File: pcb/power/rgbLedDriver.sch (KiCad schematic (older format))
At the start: 39 parts, among them Q1 MMBT3904, Q2 MMBT3904, Q3 MMBT3904, Q4 MMBT3904, Q5 MMBT3904, Q6 MMBT3904, Q7 DMG2305UX, Q8 DMG2305UX, Q9 DMG2305UX

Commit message: Did a lot of stuff. Currently working on the exact 3D models for the headers.
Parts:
- R21, R22, R23, R24, R25, R26, R30, R31, R32: footprint Resistors_SMD:R_0603_HandSoldering -> Additional:R_0603_HandSoldering_Same_As_C
- R27, R28, R29: footprint Capacitors_SMD:C_0603_HandSoldering -> Additional:R_0603_HandSoldering_Same_As_C
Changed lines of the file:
@@
 F 0 "R24" V 2680 1350 50  0000 C CNN
 F 1 "10k" V 2600 1350 50  0000 C CNN
-F 2 "Resistors_SMD:R_0603_HandSoldering" V 2530 1350 50  0001 C CNN
+F 2 "Additional:R_0603_HandSoldering_Same_As_C" V 2530 1350 50  0001 C CNN
 F 3 "http://www.yageo.com.tw/exep/pages/download/literatures/PYu-R_INT-thick_7.pdf" H 2600 1350 50  0001 C CNN
 F 4 "311-10KGRCT-ND" V 2600 1350 60  0001 C CNN "Digikey"
@@
 F 0 "R21" V 2080 2500 50  0000 C CNN
 F 1 "470R" V 2000 2500 50  0000 C CNN
-F 2 "Resistors_SMD:R_0603_HandSoldering" V 1930 2500 50  0001 C CNN
+F 2 "Additional:R_0603_HandSoldering_Same_As_C" V 1930 2500 50  0001 C CNN
 F 3 "https://industrial.panasonic.com/cdbs/www-data/pdf/RDA0000/AOA0000COL70.pdf" H 2000 2500 50  0001 C CNN
 F 4 "P20245CT-ND" V 2000 2500 60  0001 C CNN "Digikey"
@@
 F 0 "R27" V 4930 2600 50  0000 C CNN
 F 1 "0.1R" V 4850 2600 50  0000 C CNN
-F 2 "Capacitors_SMD:C_0603_HandSoldering" V 4780 2600 50  0001 C CNN
+F 2 "Additional:R_0603_HandSoldering_Same_As_C" V 4780 2600 50  0001 C CNN
 F 3 "http://media.digikey.com/pdf/Data%20Sheets/Samsung%20PDFs/RU_Series_ds.pdf" H 4850 2600 50  0001 C CNN
 F 4 "1276-6155-1-ND" V 4850 2600 60  0001 C CNN "Digikey"
@@
 F 0 "R30" V 5330 2400 50  0000 C CNN
 F 1 "4.7k" V 5250 2400 50  0000 C CNN
-F 2 "Resistors_SMD:R_0603_HandSoldering" V 5180 2400 50  0001 C CNN
+F 2 "Additional:R_0603_HandSoldering_Same_As_C" V 5180 2400 50  0001 C CNN
 F 3 "http://www.yageo.com.tw/exep/pages/download/literatures/PYu-R_INT-thick_7.pdf" H 5250 2400 50  0001 C CNN
 F 4 "311-4.7KGRCT-ND" V 5250 2400 60  0001 C CNN "Digikey"
@@
 F 0 "R22" V 2080 4550 50  0000 C CNN
 F 1 "470R" V 2000 4550 50  0000 C CNN
-F 2 "Resistors_SMD:R_0603_HandSoldering" V 1930 4550 50  0001 C CNN
+F 2 "Additional:R_0603_HandSoldering_Same_As_C" V 1930 4550 50  0001 C CNN
 F 3 "https://industrial.panasonic.com/cdbs/www-data/pdf/RDA0000/AOA0000COL70.pdf" H 2000 4550 50  0001 C CNN
 F 4 "P20245CT-ND" V 2000 4550 60  0001 C CNN "Digikey"
@@
 F 0 "R23" V 2080 6750 50  0000 C CNN
 F 1 "470R" V 2000 6750 50  0000 C CNN
-F 2 "Resistors_SMD:R_0603_HandSoldering" V 1930 6750 50  0001 C CNN
+F 2 "Additional:R_0603_HandSoldering_Same_As_C" V 1930 6750 50  0001 C CNN
 F 3 "https://industrial.panasonic.com/cdbs/www-data/pdf/RDA0000/AOA0000COL70.pdf" H 2000 6750 50  0001 C CNN
 F 4 "P20245CT-ND" V 2000 6750 60  0001 C CNN "Digikey"
@@
 F 0 "R26" V 2680 5600 50  0000 C CNN
 F 1 "10k" V 2600 5600 50  0000 C CNN
-F 2 "Resistors_SMD:R_0603_HandSoldering" V 2530 5600 50  0001 C CNN
+F 2 "Additional:R_0603_HandSoldering_Same_As_C" V 2530 5600 50  0001 C CNN
 F 3 "http://www.yageo.com.tw/exep/pages/download/literatures/PYu-R_INT-thick_7.pdf" H 2600 5600 50  0001 C CNN
 F 4 "311-10KGRCT-ND" V 2600 5600 60  0001 C CNN "Digikey"
@@
 F 0 "R25" V 2680 3400 50  0000 C CNN
 F 1 "10k" V 2600 3400 50  0000 C CNN
-F 2 "Resistors_SMD:R_0603_HandSoldering" V 2530 3400 50  0001 C CNN
+F 2 "Additional:R_0603_HandSoldering_Same_As_C" V 2530 3400 50  0001 C CNN
 F 3 "http://www.yageo.com.tw/exep/pages/download/literatures/PYu-R_INT-thick_7.pdf" H 2600 3400 50  0001 C CNN
 F 4 "311-10KGRCT-ND" V 2600 3400 60  0001 C CNN "Digikey"
@@
 F 0 "R28" V 4930 4650 50  0000 C CNN
 F 1 "0.1R" V 4850 4650 50  0000 C CNN
-F 2 "Capacitors_SMD:C_0603_HandSoldering" V 4780 4650 50  0001 C CNN
+F 2 "Additional:R_0603_HandSoldering_Same_As_C" V 4780 4650 50  0001 C CNN
 F 3 "http://media.digikey.com/pdf/Data%20Sheets/Samsung%20PDFs/RU_Series_ds.pdf" H 4850 4650 50  0001 C CNN
 F 4 "1276-6155-1-ND" V 4850 4650 60  0001 C CNN "Digikey"
@@
 F 0 "R29" V 4930 6850 50  0000 C CNN
 F 1 "0.1R" V 4850 6850 50  0000 C CNN
-F 2 "Capacitors_SMD:C_0603_HandSoldering" V 4780 6850 50  0001 C CNN
+F 2 "Additional:R_0603_HandSoldering_Same_As_C" V 4780 6850 50  0001 C CNN
 F 3 "http://media.digikey.com/pdf/Data%20Sheets/Samsung%20PDFs/RU_Series_ds.pdf" H 4850 6850 50  0001 C CNN
 F 4 "1276-6155-1-ND" V 4850 6850 60  0001 C CNN "Digikey"
@@
 F 0 "R32" V 5330 6650 50  0000 C CNN
 F 1 "4.7k" V 5250 6650 50  0000 C CNN
-F 2 "Resistors_SMD:R_0603_HandSoldering" V 5180 6650 50  0001 C CNN
+F 2 "Additional:R_0603_HandSoldering_Same_As_C" V 5180 6650 50  0001 C CNN
 F 3 "http://www.yageo.com.tw/exep/pages/download/literatures/PYu-R_INT-thick_7.pdf" H 5250 6650 50  0001 C CNN
 F 4 "311-4.7KGRCT-ND" V 5250 6650 60  0001 C CNN "Digikey"
@@
 F 0 "R31" V 5330 4450 50  0000 C CNN
 F 1 "4.7k" V 5250 4450 50  0000 C CNN
-F 2 "Resistors_SMD:R_0603_HandSoldering" V 5180 4450 50  0001 C CNN
+F 2 "Additional:R_0603_HandSoldering_Same_As_C" V 5180 4450 50  0001 C CNN
 F 3 "http://www.yageo.com.tw/exep/pages/download/literatures/PYu-R_INT-thick_7.pdf" H 5250 4450 50  0001 C CNN
 F 4 "311-4.7KGRCT-ND" V 5250 4450 60  0001 C CNN "Digikey"
@@
 $EndComp
 $Comp
-L GND #PWR022
+L GND #PWR024
 U 1 1 584185EC
 P 4850 2850
-F 0 "#PWR022" H 4850 2600 50  0001 C CNN
+F 0 "#PWR024" H 4850 2600 50  0001 C CNN
 F 1 "GND" H 4850 2700 50  0000 C CNN
 F 2 "" H 4850 2850 50  0000 C CNN
@@
 $EndComp
 $Comp
-L GND #PWR023
+L GND #PWR025
 U 1 1 584188BC
 P 4850 7100
-F 0 "#PWR023" H 4850 6850 50  0001 C CNN
+F 0 "#PWR025" H 4850 6850 50  0001 C CNN
 F 1 "GND" H 4850 6950 50  0000 C CNN
 F 2 "" H 4850 7100 50  0000 C CNN
@@
 $EndComp
 $Comp
-L GND #PWR024
+L GND #PWR026
 U 1 1 58418AC2
 P 4850 4900
-F 0 "#PWR024" H 4850 4650 50  0001 C CNN
+F 0 "#PWR026" H 4850 4650 50  0001 C CNN
 F 1 "GND" H 4850 4750 50  0000 C CNN
 F 2 "" H 4850 4900 50  0000 C CNN

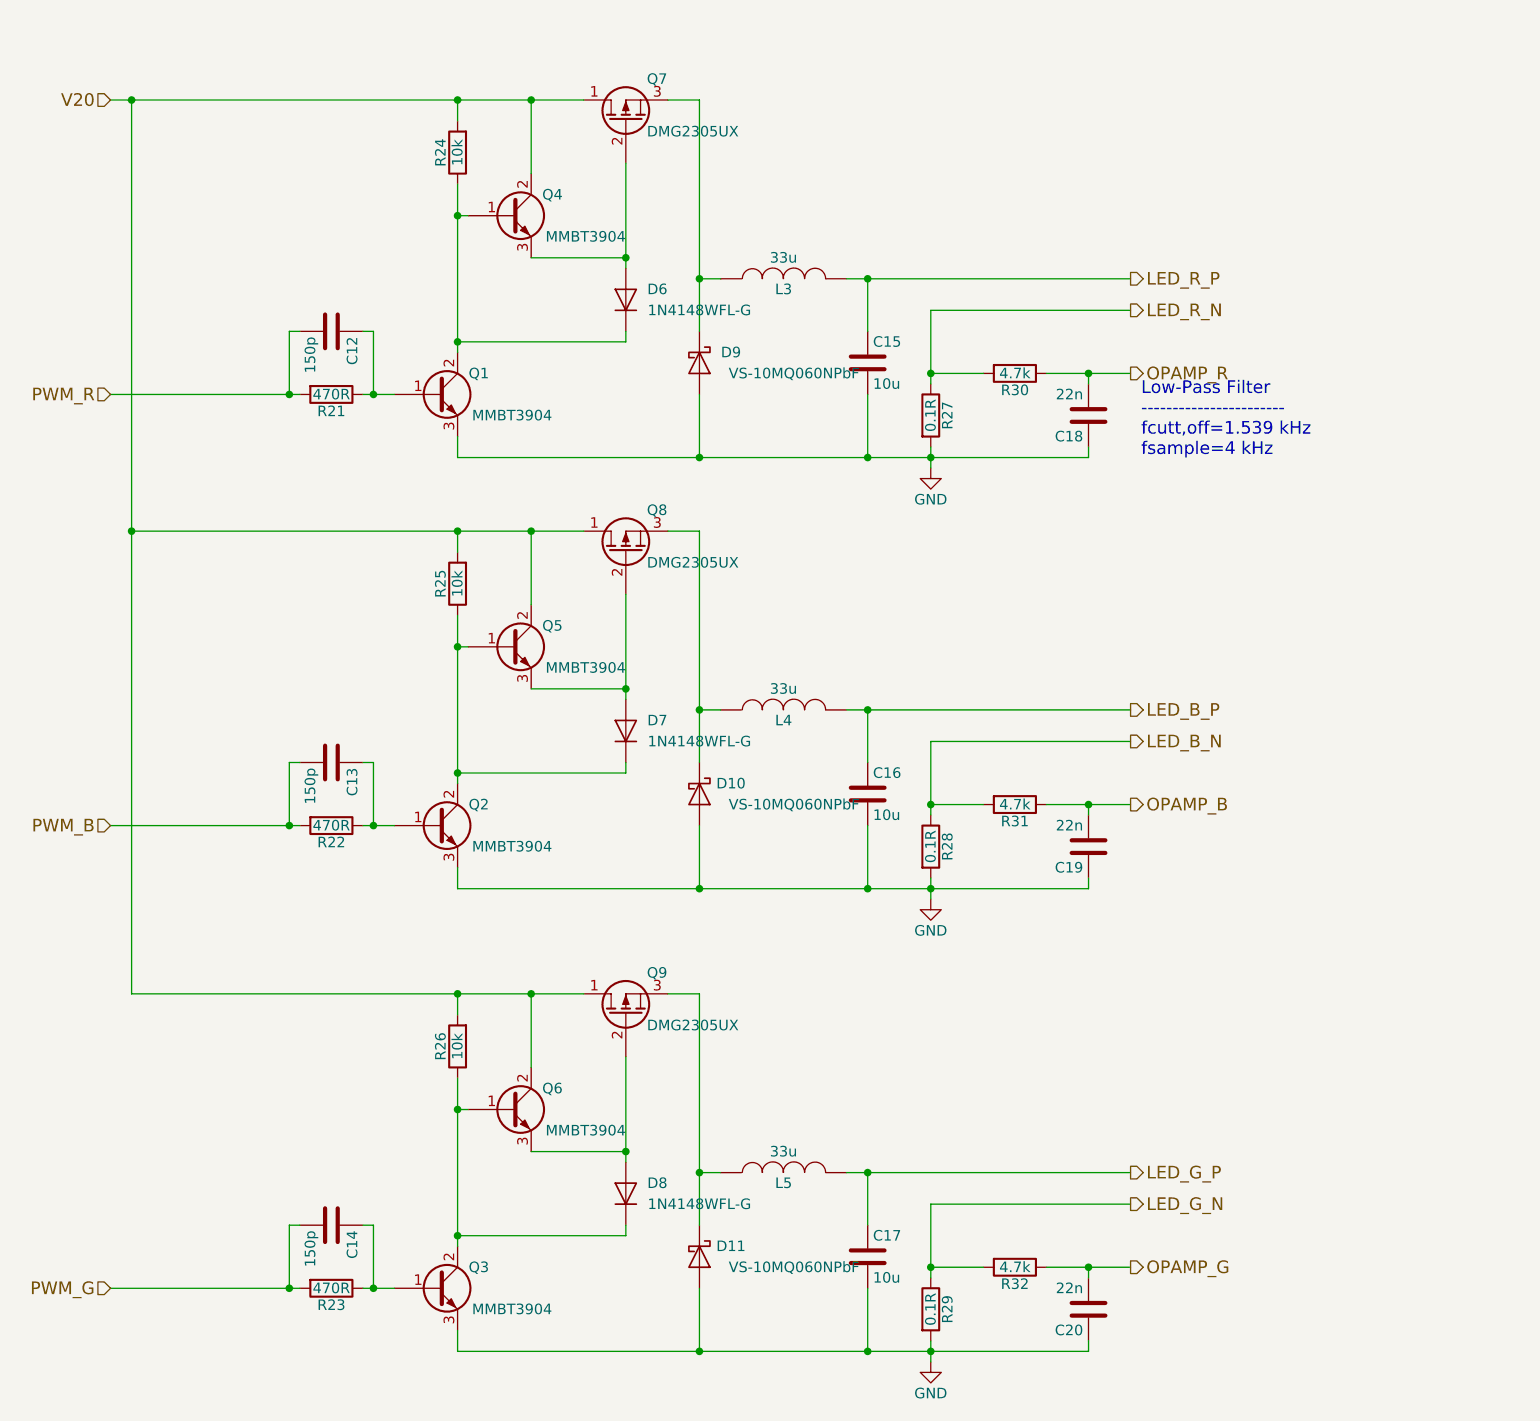
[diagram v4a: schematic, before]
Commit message: Fixed the bug. Now workin with differential amplifiers. Started over once more with the layout.
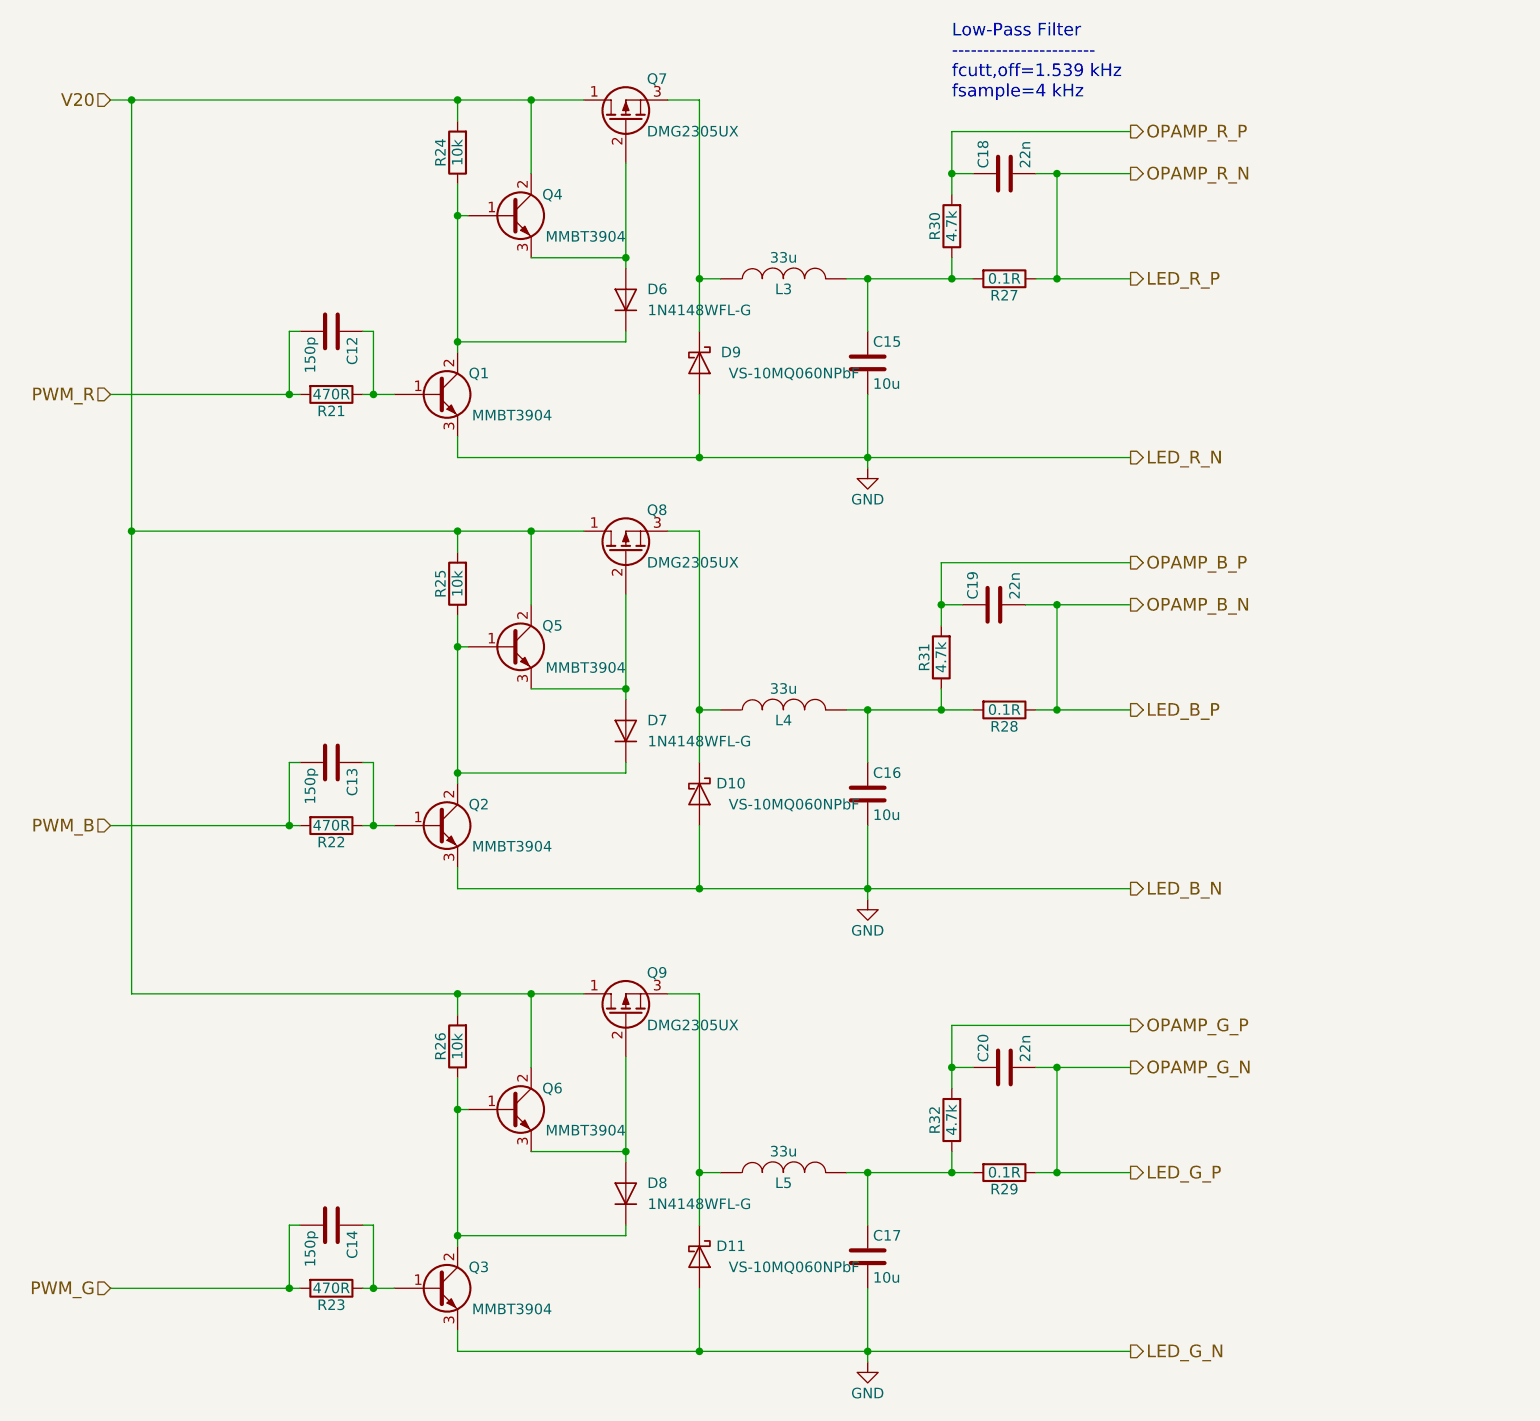
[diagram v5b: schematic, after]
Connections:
- net GND: no longer C18.1, C19.1, C20.1, R27.2, R28.2, R29.2
- net LED_B_P: now also C19.2, R28.1; no longer C16.1, L4.2
- net LED_G_P: now also C20.2, R29.1; no longer C17.1, L5.2
- net LED_R_P: now also C18.2, R27.1; no longer C15.1, L3.2
- net LED_B_N renamed OPAMP_B_P
- net OPAMP_B_P: now also C19.1; no longer R28.1
- net LED_G_N renamed OPAMP_G_P
- net OPAMP_G_P: now also C20.1; no longer R29.1
- net LED_R_N renamed OPAMP_R_P
- net OPAMP_R_P: now also C18.1; no longer R27.1
- net OPAMP_B: no longer names the net of R31.1
- net OPAMP_B: now also C16.1, L4.2, R28.2; no longer C19.2
- net OPAMP_G: no longer names the net of R32.1
- net OPAMP_G: now also C17.1, L5.2, R29.2; no longer C20.2
- net OPAMP_R: no longer names the net of R30.1
- net OPAMP_R: now also C15.1, L3.2, R27.2; no longer C18.2
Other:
- moved on the sheet: C18, C19, C20, R27, R28, R29, R30, R31, R32

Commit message: Fixed a bug.
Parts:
- C18, C19, C20: Digikey 445-8118-1-ND -> 1276-1104-1-ND
- D6, D7, D8: Digikey 1N4148WFL-G3-08GITR-ND -> (none); Farnell (none) -> 1621821
- R21, R22, R23: Digikey P20245CT-ND -> 311-470HRCT-ND
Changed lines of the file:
@@
 F 2 "Additional:R_0603_HandSoldering_Same_As_C" V 1930 2500 50  0001 C CNN
 F 3 "https://industrial.panasonic.com/cdbs/www-data/pdf/RDA0000/AOA0000COL70.pdf" H 2000 2500 50  0001 C CNN
-F 4 "P20245CT-ND" V 2000 2500 60  0001 C CNN "Digikey"
+F 4 "311-470HRCT-ND " V 2000 2500 60  0001 C CNN "Digikey"
 	1    2000 2500
 	0    1    1    0
@@
 F 2 "Capacitors_SMD:C_0603_HandSoldering" H 5238 1300 50  0001 C CNN
 F 3 "https://product.tdk.com/info/en/catalog/datasheets/mlcc_highreliability_general_en.pdf" H 5200 1450 50  0001 C CNN
-F 4 "445-8118-1-ND" H 5200 1450 60  0001 C CNN "Digikey"
+F 4 "1276-1104-1-ND" H 5200 1450 60  0001 C CNN "Digikey"
 	1    5200 1450
 	0    -1   -1   0
@@
 F 2 "Additional:SOD-123F" H 3400 2050 50  0001 C CNN
 F 3 "http://media.digikey.com/pdf/Data%20Sheets/Vishay%20Semiconductors/1N4148WFL-G.pdf" H 3400 2050 50  0001 C CNN
-F 4 "1N4148WFL-G3-08GITR-ND" V 3350 1300 60  0001 C CNN "Digikey"
+F 4 "1621821" V 3350 1300 60  0001 C CNN "Farnell"
 	1    3400 2050
 	0    -1   -1   0
@@
 F 2 "Additional:R_0603_HandSoldering_Same_As_C" V 1930 4550 50  0001 C CNN
 F 3 "https://industrial.panasonic.com/cdbs/www-data/pdf/RDA0000/AOA0000COL70.pdf" H 2000 4550 50  0001 C CNN
-F 4 "P20245CT-ND" V 2000 4550 60  0001 C CNN "Digikey"
+F 4 "311-470HRCT-ND " V 2000 4550 60  0001 C CNN "Digikey"
 	1    2000 4550
 	0    1    1    0
@@
 F 2 "Additional:R_0603_HandSoldering_Same_As_C" V 1930 6750 50  0001 C CNN
 F 3 "https://industrial.panasonic.com/cdbs/www-data/pdf/RDA0000/AOA0000COL70.pdf" H 2000 6750 50  0001 C CNN
-F 4 "P20245CT-ND" V 2000 6750 60  0001 C CNN "Digikey"
+F 4 "311-470HRCT-ND " V 2000 6750 60  0001 C CNN "Digikey"
 	1    2000 6750
 	0    1    1    0
@@
 F 2 "Additional:SOD-123F" H 3400 4100 50  0001 C CNN
 F 3 "http://media.digikey.com/pdf/Data%20Sheets/Vishay%20Semiconductors/1N4148WFL-G.pdf" H 3400 4100 50  0001 C CNN
-F 4 "1N4148WFL-G3-08GITR-ND" V 3350 3350 60  0001 C CNN "Digikey"
+F 4 "1621821" V 3350 3350 60  0001 C CNN "Farnell"
 	1    3400 4100
 	0    -1   -1   0
@@
 F 2 "Additional:SOD-123F" H 3400 6300 50  0001 C CNN
 F 3 "http://media.digikey.com/pdf/Data%20Sheets/Vishay%20Semiconductors/1N4148WFL-G.pdf" H 3400 6300 50  0001 C CNN
-F 4 "1N4148WFL-G3-08GITR-ND" V 3350 5550 60  0001 C CNN "Digikey"
+F 4 "1621821" V 3350 5550 60  0001 C CNN "Farnell"
 	1    3400 6300
 	0    -1   -1   0
@@
 F 2 "Capacitors_SMD:C_0603_HandSoldering" H 5188 3350 50  0001 C CNN
 F 3 "https://product.tdk.com/info/en/catalog/datasheets/mlcc_highreliability_general_en.pdf" H 5150 3500 50  0001 C CNN
-F 4 "445-8118-1-ND" H 5150 3500 60  0001 C CNN "Digikey"
+F 4 "1276-1104-1-ND " H 5150 3500 60  0001 C CNN "Digikey"
 	1    5150 3500
 	0    -1   -1   0
@@
 F 2 "Capacitors_SMD:C_0603_HandSoldering" H 5238 5550 50  0001 C CNN
 F 3 "https://product.tdk.com/info/en/catalog/datasheets/mlcc_highreliability_general_en.pdf" H 5200 5700 50  0001 C CNN
-F 4 "445-8118-1-ND" H 5200 5700 60  0001 C CNN "Digikey"
+F 4 "1276-1104-1-ND " H 5200 5700 60  0001 C CNN "Digikey"
 	1    5200 5700
 	0    -1   -1   0
 $EndComp
 $Comp
-L GND #PWR24
+L GND #PWR025
 U 1 1 584188BC
 P 4550 7100
-F 0 "#PWR24" H 4550 6850 50  0001 C CNN
+F 0 "#PWR025" H 4550 6850 50  0001 C CNN
 F 1 "GND" H 4550 6950 50  0000 C CNN
 F 2 "" H 4550 7100 50  0000 C CNN
@@
 $EndComp
 $Comp
-L GND #PWR23
+L GND #PWR026
 U 1 1 58418AC2
 P 4550 4900
-F 0 "#PWR23" H 4550 4650 50  0001 C CNN
+F 0 "#PWR026" H 4550 4650 50  0001 C CNN
 F 1 "GND" H 4550 4750 50  0000 C CNN
 F 2 "" H 4550 4900 50  0000 C CNN
@@
 $EndComp
 $Comp
-L GND #PWR22
+L GND #PWR027
 U 1 1 584185EC
 P 4550 2850
-F 0 "#PWR22" H 4550 2600 50  0001 C CNN
+F 0 "#PWR027" H 4550 2600 50  0001 C CNN
 F 1 "GND" H 4550 2700 50  0000 C CNN
 F 2 "" H 4550 2850 50  0000 C CNN
